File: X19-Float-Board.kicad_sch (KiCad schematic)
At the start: 2 parts

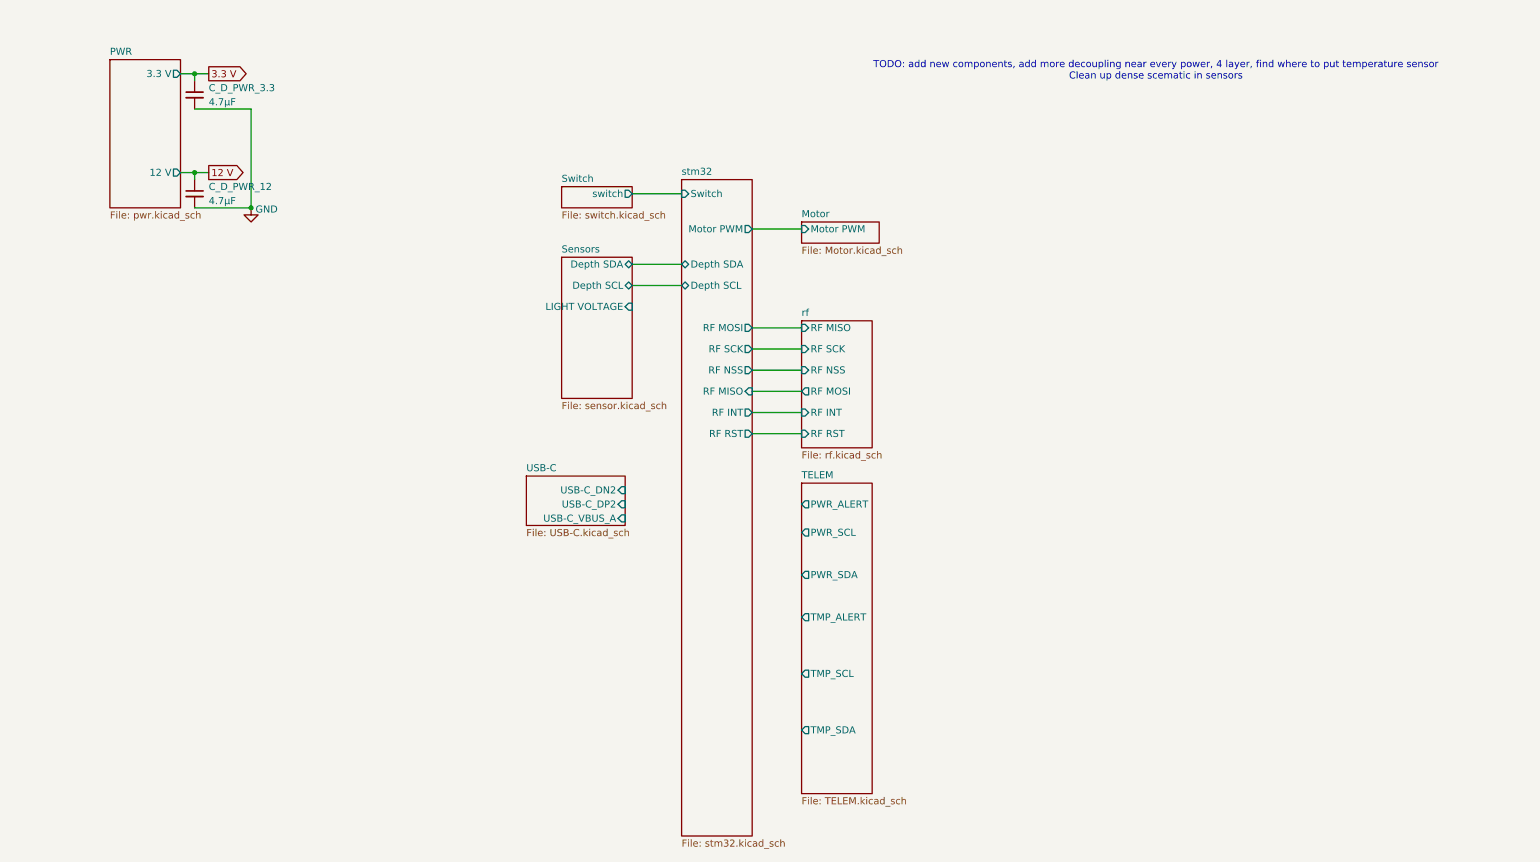
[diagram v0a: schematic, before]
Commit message: todolist update
update of the to do list on schematic
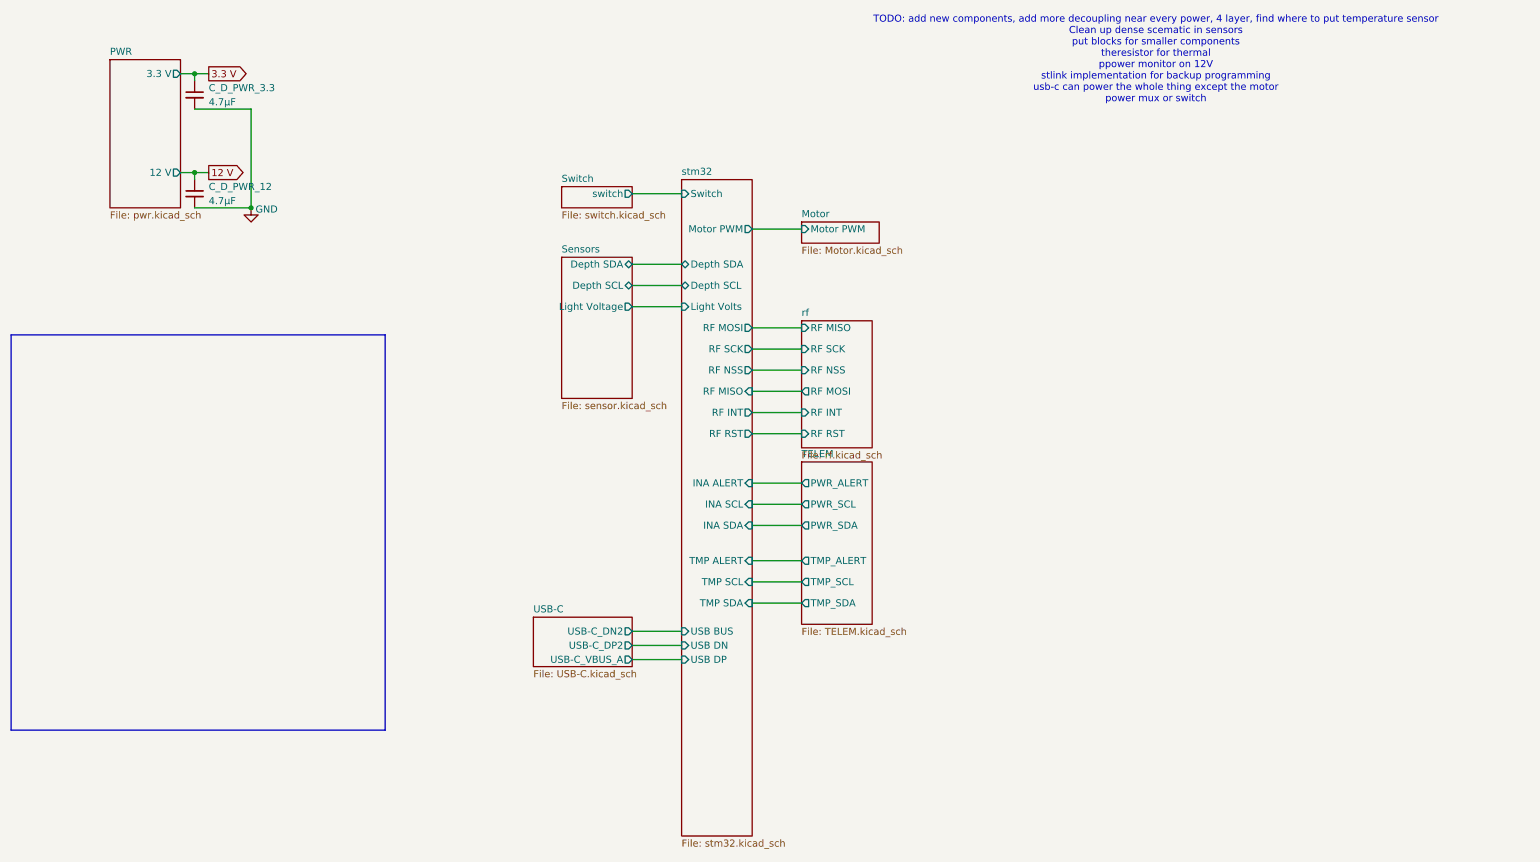
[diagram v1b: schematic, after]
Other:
- sheet Sensors ports: added Light Voltage; removed LIGHT VOLTAGE
- sheet stm32 ports: added INA ALERT, INA SCL, INA SDA, Light Volts, TMP ALERT, TMP SCL, TMP SDA, USB BUS, USB DN, USB DP; removed none
- note added: "TODO: add new components, add more decoupling near every power, 4 layer, find where to put temperature sensor Clean up dense scematic in sensors put blocks for smaller components theresistor for thermal ppower monitor on 12V stlink implementation for backup programming usb-c can power the whole thing except the motor power mux or switch"
- note removed: "TODO: add new components, add more decoupling near every power, 4 layer, find where to put temperature sensor Clean up dense scematic in sensors"
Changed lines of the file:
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@@
 		(company "Purdue ROV")
 	)
-	(text "TODO: add new components, add more decoupling near every power, 4 layer, find where to put temperature sensor\nClean up dense scematic in sensors\n"
+	(rectangle
+		(start 21.59 66.04)
+		(end 88.9 137.16)
+		(stroke
+			(width 0)
+			(type solid)
+		)
+		(fill
+			(type none)
+		)
+	)
+	(text "TODO: add new components, add more decoupling near every power, 4 layer, find where to put temperature sensor\nClean up dense scematic in sensors\nput blocks for smaller components\ntheresistor for thermal\nppower monitor on 12V\nstlink implementation for backup programming\nusb-c can power the whole thing except the motor\npower mux or switch\n\n\n"
 		(exclude_from_sim no)
 		(at 227.584 18.542 0)
@@
 	(wire
 		(pts
+			(xy 154.94 92.71) (xy 163.83 92.71)
+		)
+		(stroke
+			(width 0)
+			(type default)
+		)
+	)
+	(wire
+		(pts
+			(xy 133.35 124.46) (xy 142.24 124.46)
+		)
+		(stroke
+			(width 0)
+			(type default)
+		)
+	)
+	(wire
+		(pts
 			(xy 154.94 68.58) (xy 163.83 68.58)
 		)
@@
 	(wire
 		(pts
+			(xy 133.35 60.96) (xy 142.24 60.96)
+		)
+		(stroke
+			(width 0)
+			(type default)
+		)
+	)
+	(wire
+		(pts
 			(xy 54.61 36.83) (xy 57.15 36.83)
 		)
@@
 	(wire
 		(pts
+			(xy 154.94 114.3) (xy 163.83 114.3)
+		)
+		(stroke
+			(width 0)
+			(type default)
+		)
+	)
+	(wire
+		(pts
 			(xy 133.35 57.15) (xy 142.24 57.15)
 		)
@@
 	(wire
 		(pts
+			(xy 154.94 106.68) (xy 163.83 106.68)
+		)
+		(stroke
+			(width 0)
+			(type default)
+		)
+	)
+	(wire
+		(pts
 			(xy 52.07 19.05) (xy 54.61 19.05)
 		)
@@
 	(wire
 		(pts
+			(xy 154.94 96.52) (xy 163.83 96.52)
+		)
+		(stroke
+			(width 0)
+			(type default)
+		)
+	)
+	(wire
+		(pts
+			(xy 154.94 100.33) (xy 163.83 100.33)
+		)
+		(stroke
+			(width 0)
+			(type default)
+		)
+	)
+	(wire
+		(pts
 			(xy 133.35 53.34) (xy 142.24 53.34)
 		)
@@
 	(wire
 		(pts
+			(xy 133.35 119.38) (xy 142.24 119.38)
+		)
+		(stroke
+			(width 0)
+			(type default)
+		)
+	)
+	(wire
+		(pts
 			(xy 133.35 40.64) (xy 142.24 40.64)
 		)
@@
 	(wire
 		(pts
+			(xy 133.35 121.92) (xy 142.24 121.92)
+		)
+		(stroke
+			(width 0)
+			(type default)
+		)
+	)
+	(wire
+		(pts
 			(xy 64.77 25.4) (xy 64.77 43.18)
+		)
+		(stroke
+			(width 0)
+			(type default)
+		)
+	)
+	(wire
+		(pts
+			(xy 154.94 110.49) (xy 163.83 110.49)
 		)
 		(stroke
@@
 	)
 	(sheet
-		(at 163.83 92.71)
-		(size 12.7 55.88)
+		(at 163.83 88.9)
+		(size 12.7 29.21)
 		(exclude_from_sim no)
 		(in_bom yes)
@@
 		)
 		(property "Sheetname" "TELEM"
-			(at 163.83 91.9984 0)
+			(at 163.83 88.1884 0)
 			(show_name no)
 			(do_not_autoplace no)
@@
 		)
 		(property "Sheetfile" "TELEM.kicad_sch"
-			(at 163.83 149.1746 0)
+			(at 163.83 118.6946 0)
 			(show_name no)
 			(do_not_autoplace no)
@@
 		)
 		(pin "PWR_ALERT" output
+			(at 163.83 92.71 180)
+			(effects
+				(font
+					(size 1.27 1.27)
+				)
+				(justify left)
+			)
+		)
+		(pin "PWR_SCL" output
 			(at 163.83 96.52 180)
 			(effects
@@
 			)
 		)
-		(pin "PWR_SCL" output
-			(at 163.83 101.6 180)
-			(effects
-				(font
-					(size 1.27 1.27)
-				)
-				(justify left)
-			)
-		)
 		(pin "PWR_SDA" output
-			(at 163.83 109.22 180)
+			(at 163.83 100.33 180)
 			(effects
 				(font
@@
 		)
 		(pin "TMP_ALERT" output
-			(at 163.83 116.84 180)
+			(at 163.83 106.68 180)
 			(effects
 				(font
@@
 		)
 		(pin "TMP_SCL" output
-			(at 163.83 127 180)
+			(at 163.83 110.49 180)
 			(effects
 				(font
@@
 		)
 		(pin "TMP_SDA" output
-			(at 163.83 137.16 180)
+			(at 163.83 114.3 180)
 			(effects
 				(font
@@
 			)
 		)
-		(pin "LIGHT VOLTAGE" input
+		(pin "Light Voltage" output
 			(at 133.35 60.96 0)
 			(effects
@@
 	)
 	(sheet
-		(at 114.3 91.44)
+		(at 115.57 116.84)
 		(size 17.78 8.89)
 		(exclude_from_sim no)
@@
 		)
 		(property "Sheetname" "USB-C"
-			(at 114.3 90.7284 0)
+			(at 115.57 116.1284 0)
 			(show_name no)
 			(do_not_autoplace no)
@@
 		)
 		(property "Sheetfile" "USB-C.kicad_sch"
-			(at 114.3 100.9146 0)
+			(at 115.57 126.3146 0)
 			(show_name no)
 			(do_not_autoplace no)
@@
 			)
 		)
-		(pin "USB-C_DN2" input
-			(at 132.08 93.98 0)
-			(effects
-				(font
-					(size 1.27 1.27)
-				)
-				(justify right)
-			)
-		)
-		(pin "USB-C_DP2" input
-			(at 132.08 96.52 0)
-			(effects
-				(font
-					(size 1.27 1.27)
-				)
-				(justify right)
-			)
-		)
-		(pin "USB-C_VBUS_A" input
-			(at 132.08 99.06 0)
+		(pin "USB-C_DN2" output
+			(at 133.35 119.38 0)
+			(effects
+				(font
+					(size 1.27 1.27)
+				)
+				(justify right)
+			)
+		)
+		(pin "USB-C_DP2" output
+			(at 133.35 121.92 0)
+			(effects
+				(font
+					(size 1.27 1.27)
+				)
+				(justify right)
+			)
+		)
+		(pin "USB-C_VBUS_A" output
+			(at 133.35 124.46 0)
 			(effects
 				(font
@@
 			)
 		)
+		(pin "INA ALERT" input
+			(at 154.94 92.71 0)
+			(effects
+				(font
+					(size 1.27 1.27)
+				)
+				(justify right)
+			)
+		)
+		(pin "INA SCL" input
+			(at 154.94 96.52 0)
+			(effects
+				(font
+					(size 1.27 1.27)
+				)
+				(justify right)
+			)
+		)
+		(pin "INA SDA" input
+			(at 154.94 100.33 0)
+			(effects
+				(font
+					(size 1.27 1.27)
+				)
+				(justify right)
+			)
+		)
+		(pin "TMP ALERT" input
+			(at 154.94 106.68 0)
+			(effects
+				(font
+					(size 1.27 1.27)
+				)
+				(justify right)
+			)
+		)
+		(pin "TMP SCL" input
+			(at 154.94 110.49 0)
+			(effects
+				(font
+					(size 1.27 1.27)
+				)
+				(justify right)
+			)
+		)
+		(pin "TMP SDA" input
+			(at 154.94 114.3 0)
+			(effects
+				(font
+					(size 1.27 1.27)
+				)
+				(justify right)
+			)
+		)
+		(pin "USB BUS" input
+			(at 142.24 119.38 180)
+			(effects
+				(font
+					(size 1.27 1.27)
+				)
+				(justify left)
+			)
+		)
+		(pin "USB DN" input
+			(at 142.24 121.92 180)
+			(effects
+				(font
+					(size 1.27 1.27)
+				)
+				(justify left)
+			)
+		)
+		(pin "USB DP" input
+			(at 142.24 124.46 180)
+			(effects
+				(font
+					(size 1.27 1.27)
+				)
+				(justify left)
+			)
+		)
+		(pin "Light Volts" input
+			(at 142.24 60.96 180)
+			(effects
+				(font
+					(size 1.27 1.27)
+				)
+				(justify left)
+			)
+		)

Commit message: Updated Schematic
Updated parts of todo list for schematic
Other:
- note added: "TODO: add new components, add more decoupling near every power, 4 layer, find where to put temperature sensor Clean up dense scematic in sensors put blocks for smaller components ppower monitor on 12V stlink implementation for backup programming usb-c can power the whole thing except the motor H bridge power mux or switch Check data sheet for what to connect pins to for if it needs to be connecte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"
- note removed: "TODO: add new components, add more decoupling near every power, 4 layer, find where to put temperature sensor Clean up dense scematic in sensors put blocks for smaller components theresistor for thermal ppower monitor on 12V stlink implementation for backup programming usb-c can power the whole thing except the motor power mux or switch"
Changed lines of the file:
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@@
 		)
 	)
-	(text "TODO: add new components, add more decoupling near every power, 4 layer, find where to put temperature sensor\nClean up dense scematic in sensors\nput blocks for smaller components\ntheresistor for thermal\nppower monitor on 12V\nstlink implementation for backup programming\nusb-c can power the whole thing except the motor\npower mux or switch\n\n\n"
+	(text "TODO: add new components, add more decoupling near every power, 4 layer, find where to put temperature sensor\nClean up dense scematic in sensors\nput blocks for smaller components\nppower monitor on 12V\nstlink implementation for backup programming\nusb-c can power the whole thing except the motor\nH bridge\npower mux or switch\nCheck data sheet for what to connect pins to for if it needs to be connected to smth -> rst pull up \nstm32mx2 (later)\nFerrite bead for vref +\nH bridge drv8231\nanother ferrite bead for photoresistor divider\n10k pullup for i2c depth and battery monitor\nBattery voltage monitoring\nchange ina from 228 to 237 from standard component library\nusb TVS\ni2c pullup, all i2c is same thing cuz bus\neach alert still gets its own pin\n12v high and 12v low for ina power monitoring\nResistors and capacitor on current sensing, capacitor between vin+ and vin-\n\n\n"
 		(exclude_from_sim no)
-		(at 227.584 18.542 0)
+		(at 227.838 37.592 0)
 		(effects
 			(font

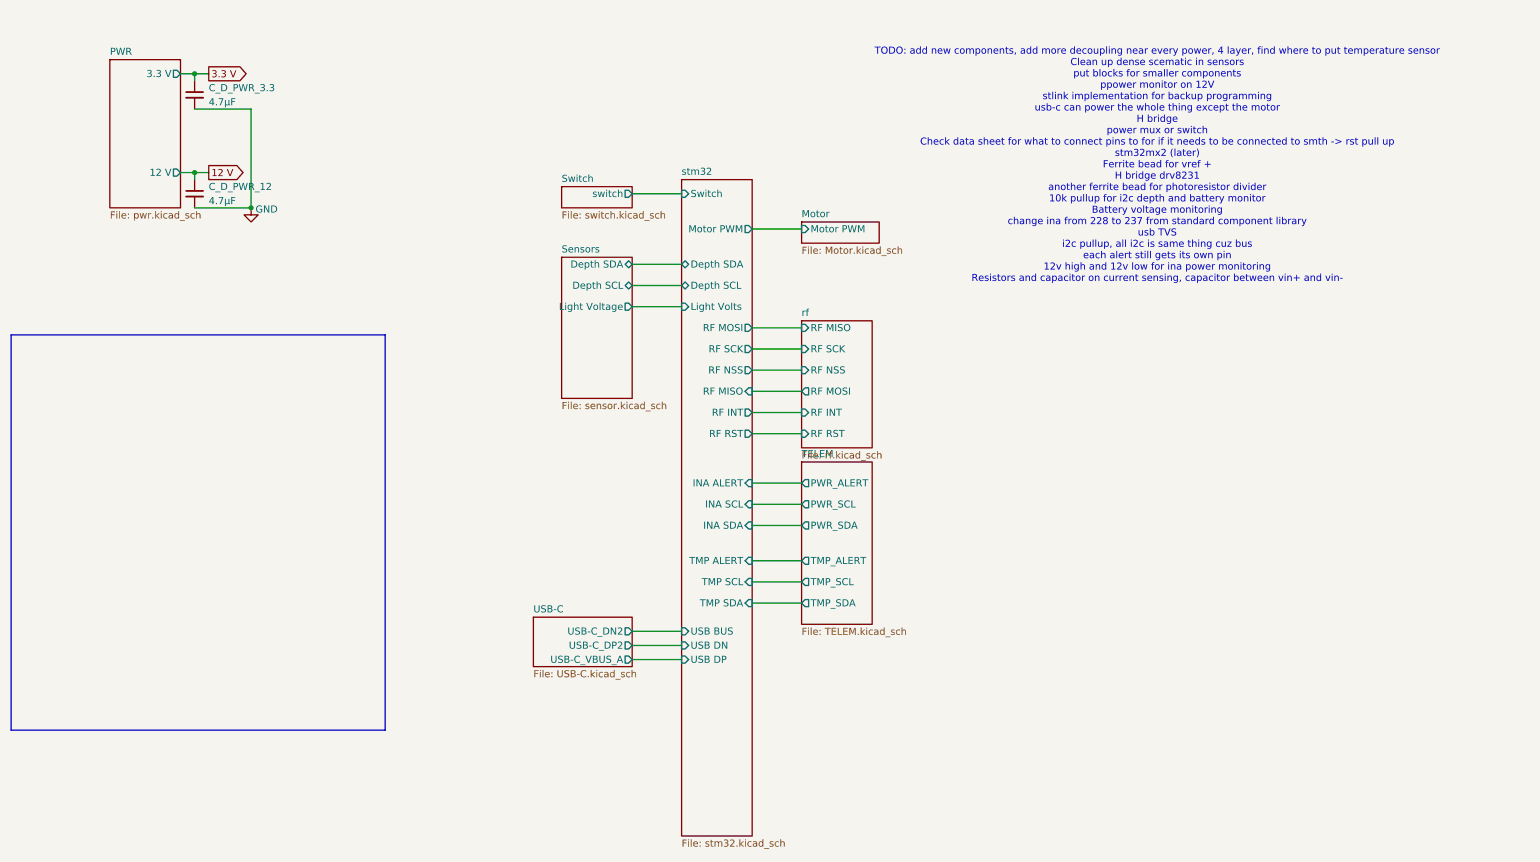
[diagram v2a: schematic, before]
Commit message: Updated Schematic
Updated schematic
Cleaned up dense portions
added H bridge
correct i2c wiring
added ferrite beads
added 12 V power monitoring
added stlink
added power mux
added power from usb
reformatted hierarichal sheets
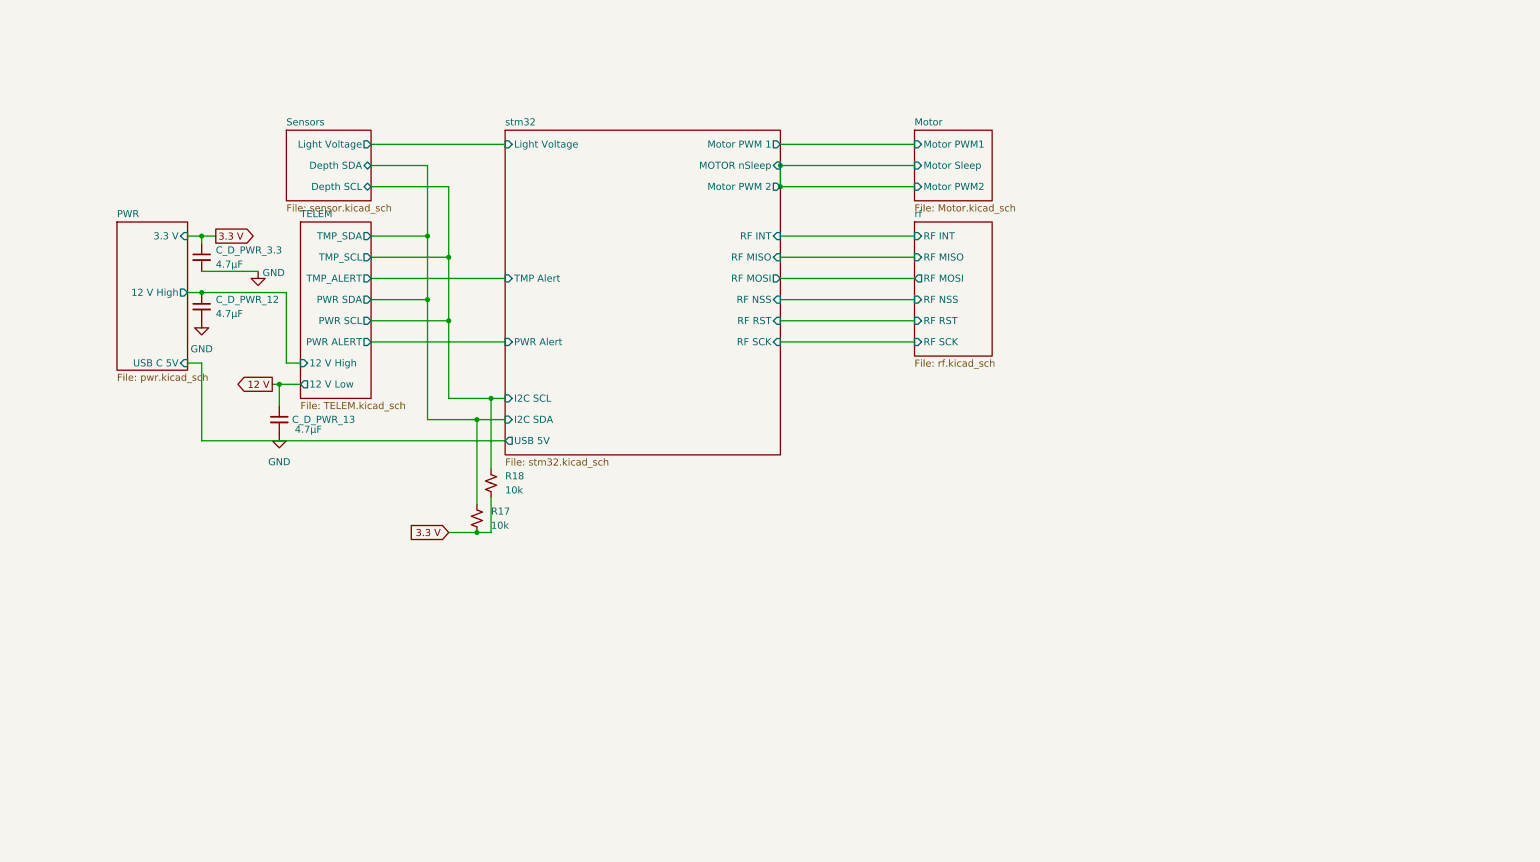
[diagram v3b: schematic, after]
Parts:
- added C_D_PWR_13: 4.7µF, Capacitor_SMD:C_0603_1608Metric, symbol Device:C_Small
- added R17, R18: 10k, symbol Device:R_Small_US
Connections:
- net 12 V: now also C_D_PWR_13.1; no longer C_D_PWR_12.1
- net 3.3 V: now also R17.2, R18.2
- net GND: now also C_D_PWR_13.2
- net Sensors/Depth SCL: now also R18.1
- net Sensors/Depth SDA: now also R17.1
- new net PWR/12 V High: C_D_PWR_12.1
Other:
- removed sheet Switch
- removed sheet USB-C
- sheet Motor ports: added Motor PWM1, Motor PWM2, Motor Sleep; removed Motor PWM
- sheet PWR ports: added 12 V High, USB C 5V; removed 12 V
- sheet TELEM ports: added 12 V High, 12 V Low, PWR ALERT, PWR SCL, PWR SDA; removed PWR_ALERT, PWR_SCL, PWR_SDA
- sheet stm32 ports: added I2C SCL, I2C SDA, Light Voltage, MOTOR nSleep, Motor PWM 1, Motor PWM 2, PWR Alert, TMP Alert, USB 5V; removed Depth SCL, Depth SDA, INA ALERT, INA SCL, INA SDA, Light Volts, Motor PWM, Switch, TMP ALERT, TMP SCL, TMP SDA, USB BUS, USB DN, USB DP
- note removed: "TODO: add new components, add more decoupling near every power, 4 layer, find where to put temperature sensor Clean up dense scematic in sensors put blocks for smaller components ppower monitor on 12V stlink implementation for backup programming usb-c can power the whole thing except the motor H bridge power mux or switch Check data sheet for what to connect pins to for if it needs to be connecte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"
- moved on the sheet: C_D_PWR_3.3

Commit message: footprints
footprints
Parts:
- added J3: SZ conn, symbol Connector:Conn_01x04_Pin
- added R19, R20: 10k, symbol Device:R_Small_US
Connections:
- net 3.3 V: now also R19.2, R20.2
- net GND: now also J3.4 (Pin_4)
- net PWR/USB C 5V: now also J3.3 (Pin_3)
- net Sensors/Depth SCL: now also J3.1 (Pin_1)
- net Sensors/Depth SDA: now also J3.2 (Pin_2)
- net TELEM/PWR ALERT: now also R20.1
- net TELEM/TMP_ALERT: now also R19.1
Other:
- moved on the sheet: R18
